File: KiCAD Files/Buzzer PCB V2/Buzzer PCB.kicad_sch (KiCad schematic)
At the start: 18 parts, among them J1 2600mAh LiPo JST-PH bottom, J10 Adafruit ESP32 Feather V2, J11 OLED FeatherWing, J2 Legacy SW_BAT/GND out, J3 SD card module 18x18 swapped, J4 Legacy D13 test pad, J5 GPS M100 Mini 15x15, J6 BMP390/BMP5xx top pads, J7 SHT41 top pads, Q1 S8050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

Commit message: V2 with sparkfun
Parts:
- removed J10: Adafruit ESP32 Feather V2, Vario_Buzzer_V2:Feather_28_Header_Separate, symbol Vario_Buzzer_V2:Feather_28_Header
- removed J11: OLED FeatherWing, Vario_Buzzer_V2:OLED_FeatherWing_28_Header, symbol Vario_Buzzer_V2:Feather_28_Header
- added J10: SparkFun Thing Plus ESP32 WROOM-C USB-C, Vario_Buzzer_V2:SparkFun_Thing_Plus_ESP32_WROOM_C_Header, symbol Vario_Buzzer_V2:SparkFun_Thing_Plus_ESP32_WROOM_C
- added J11: SparkFun Qwiic OLED 1.3in, Vario_Buzzer_V2:SparkFun_Qwiic_OLED_1p3_Module, symbol Vario_Buzzer_V2:SparkFun_Qwiic_OLED_1p3
- added SW2: BACK, Vario_Buzzer_V2:Ant_Display_SW_PUSH_6mm_H5mm, symbol Vario_Buzzer_V2:Ant_Display_Button
- added SW3: NEXT, Vario_Buzzer_V2:Ant_Display_SW_PUSH_6mm_H5mm, symbol Vario_Buzzer_V2:Ant_Display_Button
- added SW4: DOWN, Vario_Buzzer_V2:Ant_Display_SW_PUSH_6mm_H5mm, symbol Vario_Buzzer_V2:Ant_Display_Button
- added SW5: UP, Vario_Buzzer_V2:Ant_Display_SW_PUSH_6mm_H5mm, symbol Vario_Buzzer_V2:Ant_Display_Button
- J3: value SD card module 18x18 swapped -> Optional SD module 18x18 swapped
- J5: value GPS M100 Mini 15x15 -> HGLRC M100 Mini GPS
- SW1: value SS12D00G5 -> SS12D00G5 power switch
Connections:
- net GPS_RX_FEATHER_TX is gone; now on net GND: J5.1 (RX)
- net GPS_TX_FEATHER_RX is gone; now on net 3V3: J5.2 (TX)
- net 3V3: now also J11.3 (SDA); no longer J5.3 (TX)
- net GND: now also SW1.1 (ON), J11.4 (SCL), SW2.1 (BTN), SW3.1 (BTN), SW4.1 (BTN), SW5.1 (BTN); no longer J5.4 (RX)
- net SCL: now also J11.1 (GND)
- net SDA: now also J11.2 (VDD/3V3)
- net D13 renamed D13_BUZZER_GPIO13
- net D13_BUZZER_GPIO13: now also J10.15 (RX ESP16)
- net SD_CS_D10_IO27 renamed SD_CS_GPIO2
- net SD_CS_GPIO2: now also J10.23 (A1/ESP25)
- new net BTN_BACK_GPIO3: J10.19 (A5/ESP35), SW2.2 (GND)
- new net BTN_DOWN_GPIO5: J10.21 (A3/ESP39), SW4.2 (GND)
- new net BTN_NEXT_GPIO4: J10.20 (A4/ESP36), SW3.2 (GND)
- new net BTN_UP_GPIO21: J10.22 (A2/ESP34), SW5.2 (GND)
- new net GPS_RX_THING_TX: J10.14 (TX ESP17), J5.4 (GND)
- new net GPS_TX_THING_RX: J10.9 (D13/ESP13 STAT), J5.3 (VCC)
- no-connect marks 36 -> 2
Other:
- note added: "Ant Display tactile switch pad geometry and button net names are copied; UP net is routed to Thing FREEBIE/ESP4 to keep SDA free for I2C."
- note added: "Buzzer circuit and copied original Buzzer PCB passives/JST/slide-switch footprints are preserved; PCB remains placement-only with no traces."
- note added: "HGLRC M100 footprint uses manual pad order RX TX VCC GND; VCC is tied to 3V3 per HGLRC 3.3V-5V product spec."
- note added: "SparkFun Thing Plus and SparkFun Qwiic OLED replace the Feather/FeatherWing. OLED uses direct 3V3/GND/SDA/SCL pads; no PCB Qwiic port is placed."
- note added: "SparkFun Thing Plus pinout and module outline are from SparkFun Eagle hardware. Onboard microSD exists; J3 is optional external SPI SD using GPIO2 as CS."
- note removed: "BMP/SHT footprints use Adafruit EagleCAD breakout geometry; top-facing modules solder from PCB backside."
- note removed: "J3 SD pin order is reversed: 1 GND, 2 MISO, 3 CLK, 4 MOSI, 5 CS, 6 3V3."
- note removed: "Reused buzzer/JST/switch/passive footprints and pad nets are copied from the original Buzzer PCB board file."
- note removed: "U1 TP4057: USB-C edge is opposite BAT+/BAT- pads. BAT_IN charges before SW1; SW_BAT feeds Feather VBAT and buzzer."
- note removed: "V2 separates Feather and OLED FeatherWing onto J10/J11. No separate I2C cable connector is placed on this PCB."
- title: Feather Vario Buzzer / Sensor Interposer PCB V2 -> SparkFun Thing Plus Vario Buzzer / Sensor Interposer PCB V2

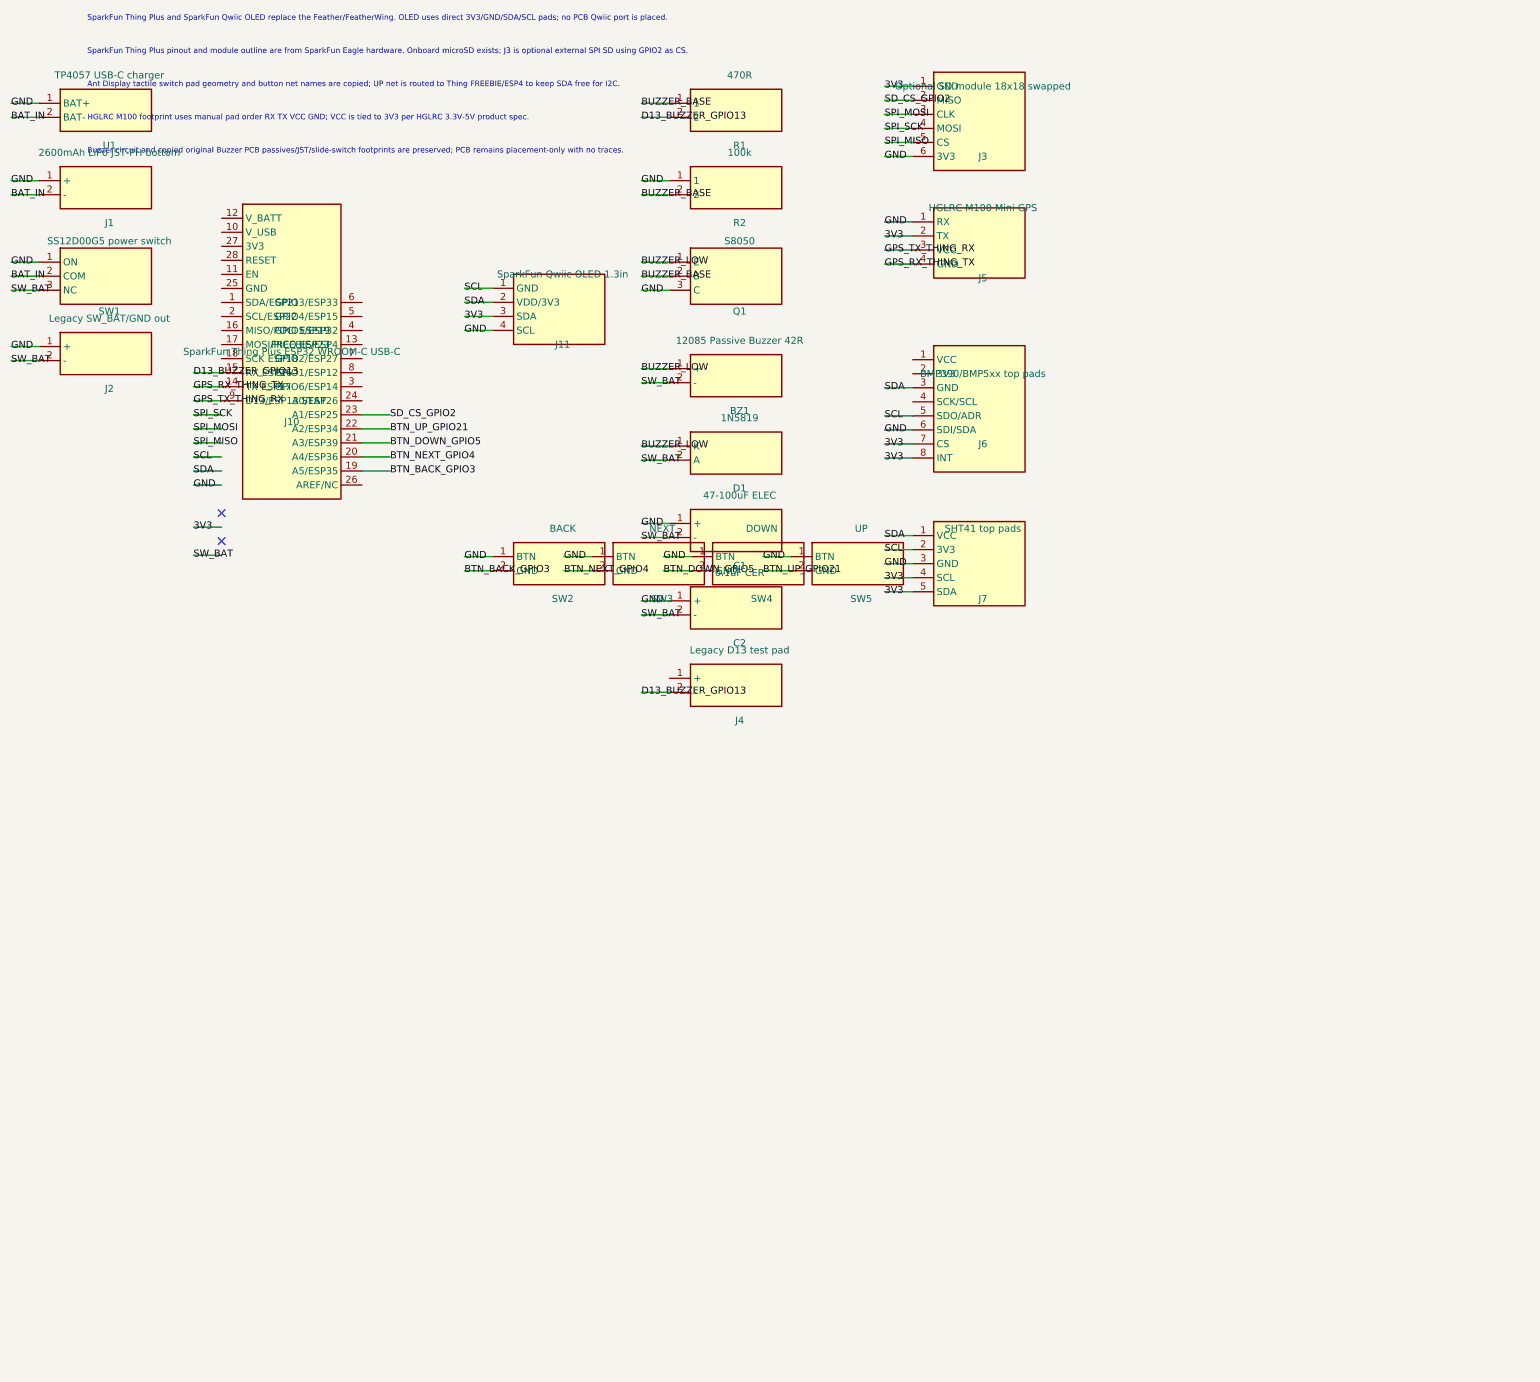
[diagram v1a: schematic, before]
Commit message: Restore KiCad component references and footprints
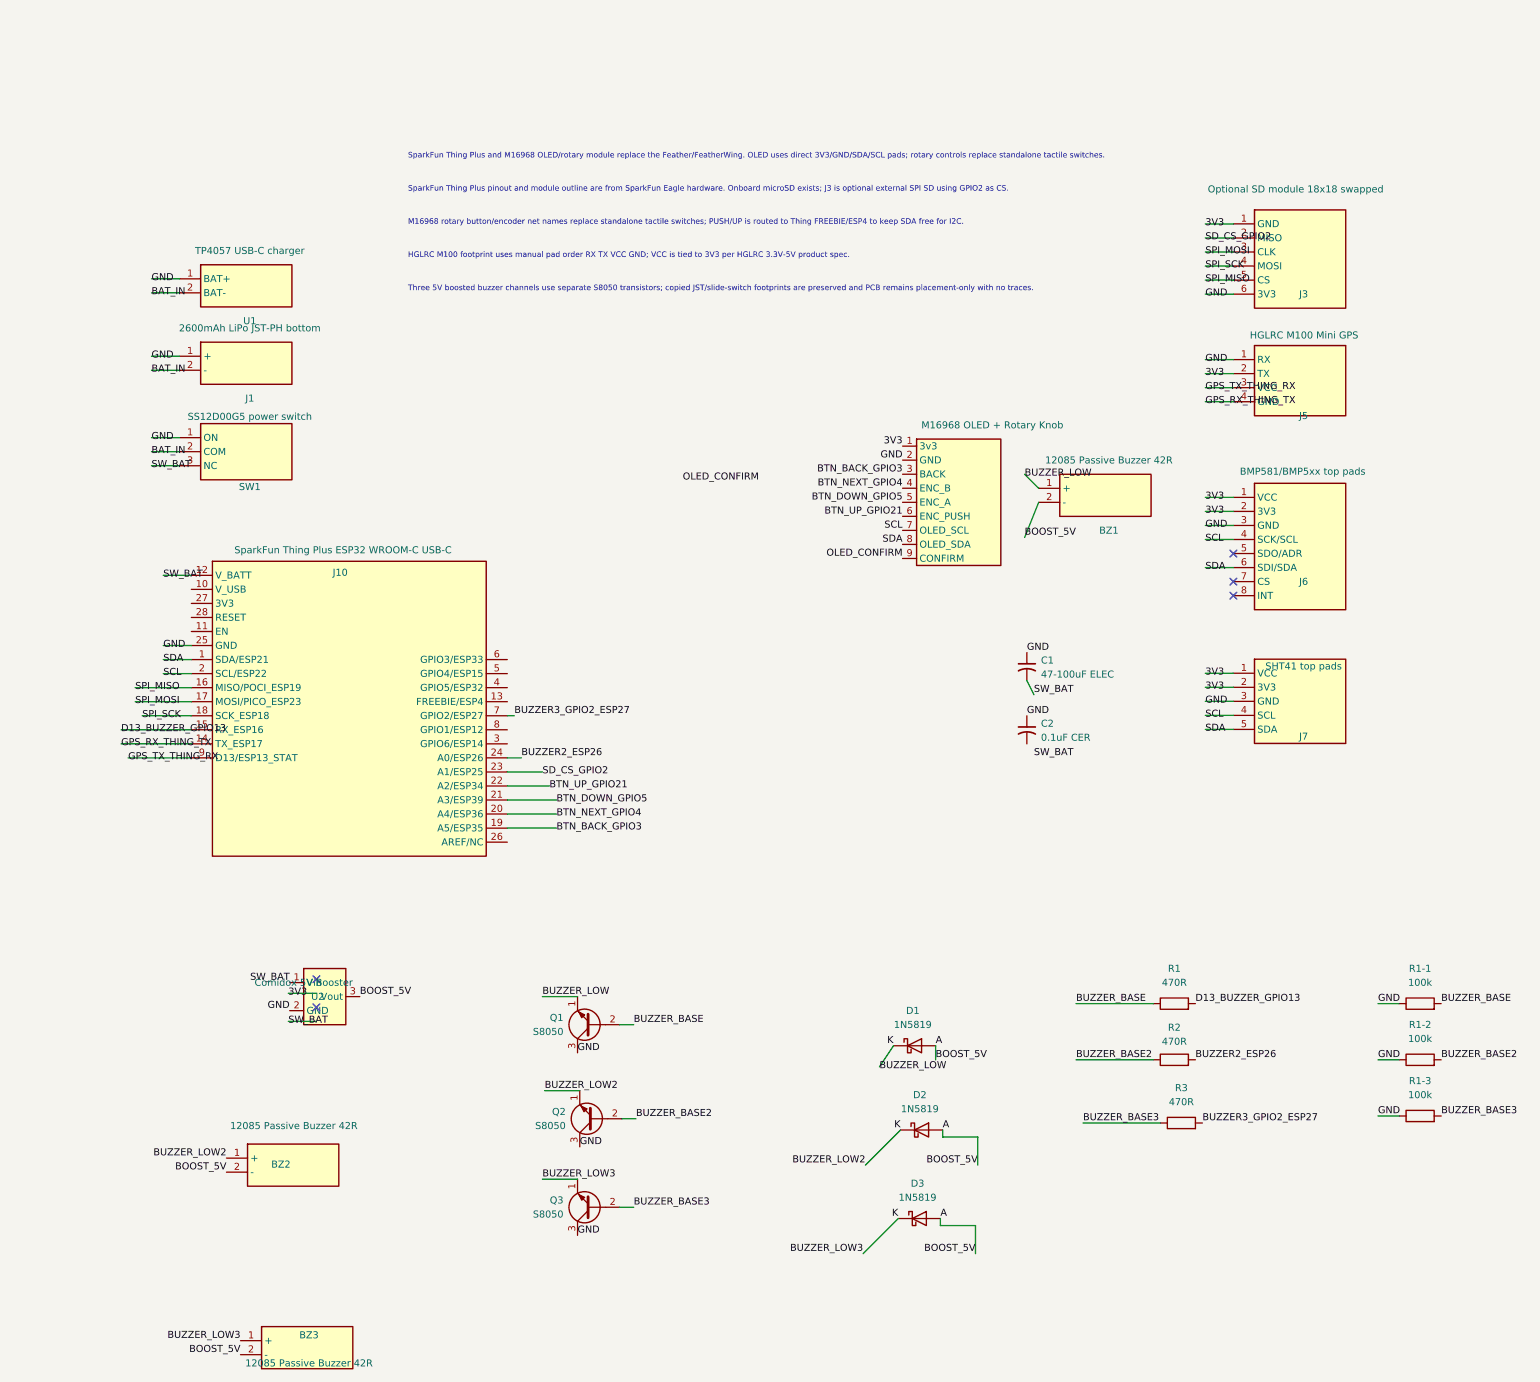
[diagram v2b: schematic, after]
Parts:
- removed C1: 47-100uF ELEC, Capacitor_THT:CP_Radial_D5.0mm_P2.00mm, symbol Vario_Buzzer_V2:Capacitor_2
- removed C2: 0.1uF CER, Capacitor_THT:C_Disc_D3.0mm_W1.6mm_P2.50mm, symbol Vario_Buzzer_V2:Capacitor_2
- removed D1: 1N5819, Diode_THT:D_DO-41_SOD81_P10.16mm_Horizontal, symbol Vario_Buzzer_V2:Diode_2
- removed J11: SparkFun Qwiic OLED 1.3in, Vario_Buzzer_V2:SparkFun_Qwiic_OLED_1p3_Module, symbol Vario_Buzzer_V2:SparkFun_Qwiic_OLED_1p3
- removed J2: Legacy SW_BAT/GND out, Connector_JST:JST_PH_S2B-PH-K_1x02_P2.00mm_Horizontal, symbol Vario_Buzzer_V2:Conn_2
- removed J4: Legacy D13 test pad, Connector_PinHeader_2.54mm:PinHeader_1x01_P2.54mm_Vertical, symbol Vario_Buzzer_V2:Conn_2
- removed Q1: S8050, Package_TO_SOT_THT:TO-92_Inline_Wide_Formed, symbol Vario_Buzzer_V2:NPN_EBC_3
- removed R1: 470R, Resistor_THT:R_Axial_DIN0207_L6.3mm_D2.5mm_P7.62mm_Horizontal, symbol Vario_Buzzer_V2:Resistor_2
- removed R2: 100k, Resistor_THT:R_Axial_DIN0207_L6.3mm_D2.5mm_P7.62mm_Horizontal, symbol Vario_Buzzer_V2:Resistor_2
- removed SW2: BACK, Vario_Buzzer_V2:Ant_Display_SW_PUSH_6mm_H5mm, symbol Vario_Buzzer_V2:Ant_Display_Button
- removed SW3: NEXT, Vario_Buzzer_V2:Ant_Display_SW_PUSH_6mm_H5mm, symbol Vario_Buzzer_V2:Ant_Display_Button
- removed SW4: DOWN, Vario_Buzzer_V2:Ant_Display_SW_PUSH_6mm_H5mm, symbol Vario_Buzzer_V2:Ant_Display_Button
- removed SW5: UP, Vario_Buzzer_V2:Ant_Display_SW_PUSH_6mm_H5mm, symbol Vario_Buzzer_V2:Ant_Display_Button
- added BZ2, BZ3: 12085 Passive Buzzer 42R, Buzzer_Beeper:Buzzer_12x8.5mm_P7.62mm_Custom, symbol Vario_Buzzer_V2:Buzzer_2
- added C1: 47-100uF ELEC, Capacitor_THT:CP_Radial_D5.0mm_P2.00mm, symbol Device:C_Small_US
- added C2: 0.1uF CER, Vario_Buzzer_V2:Ceramic_Cap_0.1uF_P5.00mm_V1, symbol Device:C_Small_US
- added D1, D2, D3: 1N5819, Diode_THT:D_DO-41_SOD81_P10.16mm_Horizontal, symbol Diode:1N5819
- added J11: M16968 OLED + Rotary Knob, Vario_Buzzer_V2:OLED_M16968_59x35_9Pin, symbol Vario_Buzzer_V2:M16968_OLED_RotaryKnob_9
- added Q1, Q2, Q3: S8050, Package_TO_SOT_THT:TO-92_Inline, symbol Transistor_BJT:S8050
- added R1, R2, R3: 470R, Resistor_THT:R_Axial_DIN0207_L6.3mm_D2.5mm_P10.16mm_Horizontal, symbol Device:R
- added R1-1, R1-2, R1-3: 100k, Resistor_THT:R_Axial_DIN0207_L6.3mm_D2.5mm_P10.16mm_Horizontal, symbol Device:R
- added U2: Comidox 5V Booster, Vario_Buzzer_V2:Comidox_5V_Booster_10.75x10.75_3Pin, symbol Vario_Buzzer_V2:Comidox_5V_Booster_3
- J6: value BMP390/BMP5xx top pads -> BMP581/BMP5xx top pads
- U1: footprint Vario_Buzzer_V2:TP4057_Module_18.2x12.3 -> Vario_Buzzer_V2:TP4057_Module_12.2x18.5
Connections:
- net 3V3: now also J6.1 (VCC), J6.2 (3V3), J7.1 (VCC), J7.2 (3V3), J11.1 (3v3); no longer J6.7 (CS), J6.8 (INT), J7.4 (SCL), J7.5 (SDA)
- net BTN_BACK_GPIO3: now also J11.3 (BACK)
- net BTN_DOWN_GPIO5: now also J11.5 (ENC_A)
- net BTN_NEXT_GPIO4: now also J11.4 (ENC_B)
- net BTN_UP_GPIO21: now also J11.6 (ENC_PUSH)
- net BUZZER_BASE: now also Q1.2 (B), R1-1.2, R1.1
- net BUZZER_LOW: now also BZ2.1 (+), BZ3.1 (+), D1.1 (K), D2.1 (K), D3.1 (K), Q1.1 (E), Q2.1 (E), Q3.1 (E)
- net D13_BUZZER_GPIO13: now also R1.2
- net GND: now also J10.25 (GND), J6.3 (GND), C1.1, C2.1, J11.2 (GND), Q1.3 (C), Q2.3 (C), Q3.3 (C), R1-1.1, R1-2.1, R1-3.1, U2.2 (GND); no longer J6.6 (SDI/SDA)
- net SCL: now also J10.2 (SCL/ESP22), J6.4 (SCK/SCL), J7.4 (SCL), J11.7 (OLED_SCL); no longer J6.5 (SDO/ADR), J7.2 (3V3)
- net SDA: now also J10.1 (SDA/ESP21), J6.6 (SDI/SDA), J7.5 (SDA), J11.8 (OLED_SDA); no longer J6.3 (GND), J7.1 (VCC)
- net SPI_MISO: now also J10.16 (MISO/POCI_ESP19)
- net SPI_MOSI: now also J10.17 (MOSI/PICO_ESP23)
- net SPI_SCK: now also J10.18 (SCK_ESP18)
- net SW_BAT: now also J10.12 (V_BATT), C1.2, U2.1 (Vin); no longer BZ1.2 (-)
- net BUZZER2_ESP26: now reaches J10.24 (A0/ESP26)
- net BUZZER2_ESP26: now also R2.2
- net BUZZER3_GPIO2_ESP27: now reaches J10.7 (GPIO2/ESP27)
- net BUZZER3_GPIO2_ESP27: now also R3.2
- new net A: BZ1.2 (-), BZ2.2 (-), BZ3.2 (-), D1.2 (A), D2.2 (A), D3.2 (A), U2.3 (Vout)
- new net BUZZER_BASE2: Q2.2 (B), R1-2.2, R2.1
- new net BUZZER_BASE3: Q3.2 (B), R1-3.2, R3.1
- new net OLED_CONFIRM: J11.9 (CONFIRM)
- no-connect marks 2 -> 5
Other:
- note added: "M16968 rotary button/encoder net names replace standalone tactile switches; PUSH/UP is routed to Thing FREEBIE/ESP4 to keep SDA free for I2C."
- note added: "SparkFun Thing Plus and M16968 OLED/rotary module replace the Feather/FeatherWing. OLED uses direct 3V3/GND/SDA/SCL pads; rotary controls replace standalone tactile switches."
- note added: "Three 5V boosted buzzer channels use separate S8050 transistors; copied JST/slide-switch footprints are preserved and PCB remains placement-only with no traces."
- note removed: "Ant Display tactile switch pad geometry and button net names are copied; UP net is routed to Thing FREEBIE/ESP4 to keep SDA free for I2C."
- note removed: "Buzzer circuit and copied original Buzzer PCB passives/JST/slide-switch footprints are preserved; PCB remains placement-only with no traces."
- note removed: "SparkFun Thing Plus and SparkFun Qwiic OLED replace the Feather/FeatherWing. OLED uses direct 3V3/GND/SDA/SCL pads; no PCB Qwiic port is placed."
- moved on the sheet: BZ1, J1, J10, J3, J5, J6, J7, SW1, U1

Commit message: asd
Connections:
- net 3V3: no longer J6.2 (3V3), J7.2 (3V3)
- net OLED_CONFIRM: now also J10.13 (FREEBIE/ESP4)
- no-connect marks 5 -> 6
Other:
- moved on the sheet: BZ1, BZ2
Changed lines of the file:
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@@
 	)
 	(no_connect
+		(at 62.23 223.52)
+	)
+	(no_connect
 		(at 59.45 191.17)
 	)
@@
 	(wire
 		(pts
-			(xy 187.55 111.26) (xy 190.09 104.91)
+			(xy 44.45 233.68) (xy 46.99 227.33)
 		)
 		(stroke
@@
 	(wire
 		(pts
-			(xy 187.55 99.83) (xy 190.09 102.37)
+			(xy 44.45 222.25) (xy 46.99 224.79)
 		)
 		(stroke
@@
 	(wire
 		(pts
+			(xy 43.18 242.57) (xy 43.18 241.3)
+		)
+		(stroke
+			(width 0)
+			(type default)
+		)
+	)
+	(wire
+		(pts
 			(xy 31.75 135.89) (xy 36.83 135.89)
 		)
@@
 	(wire
 		(pts
-			(xy 178.66 235.72) (xy 172.31 235.72)
+			(xy 48.26 242.57) (xy 43.18 242.57)
 		)
 		(stroke
@@
 	(wire
 		(pts
-			(xy 178.66 240.8) (xy 178.66 235.72)
+			(xy 178.66 235.72) (xy 172.31 235.72)
 		)
 		(stroke
@@
 	(wire
 		(pts
-			(xy 116.84 199.39) (xy 114.3 199.39)
+			(xy 178.66 240.8) (xy 178.66 235.72)
 		)
 		(stroke
@@
 	(wire
 		(pts
-			(xy 172.72 219.71) (xy 172.72 218.44)
+			(xy 116.84 199.39) (xy 114.3 199.39)
 		)
 		(stroke
@@
 	(wire
 		(pts
-			(xy 29.62 95.75) (xy 34.7 95.75)
+			(xy 172.72 219.71) (xy 172.72 218.44)
 		)
 		(stroke
@@
 	(wire
 		(pts
-			(xy 196.85 195.58) (xy 210.82 195.58)
+			(xy 43.18 246.38) (xy 48.26 245.11)
 		)
 		(stroke
@@
 	(wire
 		(pts
-			(xy 158.34 240.8) (xy 164.69 234.45)
+			(xy 29.62 95.75) (xy 34.7 95.75)
 		)
 		(stroke
@@
 	(wire
 		(pts
-			(xy 220.23 59.63) (xy 225.31 59.63)
+			(xy 196.85 195.58) (xy 210.82 195.58)
 		)
 		(stroke
@@
 	(wire
 		(pts
-			(xy 29.62 64.48) (xy 34.7 64.48)
+			(xy 158.34 240.8) (xy 164.69 234.45)
 		)
 		(stroke
@@
 	(wire
 		(pts
-			(xy 220.23 138.36) (xy 225.31 138.36)
+			(xy 220.23 59.63) (xy 225.31 59.63)
 		)
 		(stroke
@@
 	(wire
 		(pts
-			(xy 220.23 104.01) (xy 225.31 104.01)
+			(xy 29.62 64.48) (xy 34.7 64.48)
 		)
 		(stroke
@@
 	(wire
 		(pts
-			(xy 220.23 106.55) (xy 225.31 106.55)
+			(xy 220.23 104.01) (xy 225.31 104.01)
 		)
 		(stroke
@@
 		)
 	)
-	(label "3V3"
-		(at 220.23 138.36 0)
-		(effects
-			(font
-				(size 1.27 1.27)
-			)
-		)
-	)
 	(label "BUZZER_BASE"
 		(at 262.89 195.58 0)
@@
 		)
 	)
-	(label "3V3"
-		(at 220.23 106.55 0)
-		(effects
-			(font
-				(size 1.27 1.27)
-			)
-		)
-	)
 	(label "BOOST_5V"
 		(at 171.45 205.74 0)
@@
 	)
 	(label "BUZZER_LOW"
-		(at 187.55 99.83 0)
+		(at 44.45 222.25 0)
 		(effects
 			(font
@@
 	)
 	(label "BOOST_5V"
-		(at 187.55 111.26 0)
+		(at 44.45 233.68 0)
 		(effects
 			(font
@@
 	)
 	(label "BUZZER_LOW2"
-		(at 43.18 223.52 180)
+		(at 43.18 241.3 180)
 		(effects
 			(font
@@
 	)
 	(label "BOOST_5V"
-		(at 43.18 226.06 180)
+		(at 43.18 246.38 180)
 		(effects
 			(font
@@
 		)
 	)
+	(label "OLED_CONFIRM"
+		(at 93.98 140.97 0)
+		(effects
+			(font
+				(size 1.27 1.27)
+			)
+			(justify left bottom)
+		)
+	)
 	(label "BUZZER_BASE"
 		(at 196.85 195.58 0)
@@
 	(symbol
 		(lib_id "Vario_Buzzer_V2:Buzzer_2")
-		(at 202.79 103.64 0)
+		(at 59.69 226.06 0)
 		(unit 1)
 		(body_style 1)
@@
 		(dnp no)
 		(property "Reference" "BZ1"
-			(at 202.79 109.99 0)
+			(at 59.69 232.41 0)
 			(show_name no)
 			(do_not_autoplace no)
@@
 		)
 		(property "Value" "12085 Passive Buzzer 42R"
-			(at 202.79 97.29 0)
+			(at 59.436 218.948 0)
 			(show_name no)
 			(do_not_autoplace no)
@@
 		)
 		(property "Footprint" "Buzzer_Beeper:Buzzer_12x8.5mm_P7.62mm_Custom"
-			(at 202.79 103.64 0)
+			(at 59.69 226.06 0)
 			(hide yes)
 			(show_name no)
@@
 		)
 		(property "Datasheet" ""
-			(at 66.79 21.64 0)
+			(at -76.31 144.06 0)
 			(hide yes)
 			(show_name no)
@@
 		)
 		(property "Description" ""
-			(at 202.79 103.64 0)
+			(at 59.69 226.06 0)
 			(show_name no)
 			(do_not_autoplace no)
@@
 		)
 		(property "Value" "12085 Passive Buzzer 42R"
-			(at 58.11 260.61 0)
+			(at 57.15 251.968 0)
 			(show_name no)
 			(do_not_autoplace no)
@@
 	(symbol
 		(lib_id "Vario_Buzzer_V2:Buzzer_2")
-		(at 55.88 224.79 0)
+		(at 60.96 243.84 0)
 		(unit 1)
 		(body_style 1)
@@
 		(dnp no)
 		(property "Reference" "BZ2"
-			(at 53.03 224.65 0)
+			(at 58.11 243.7 0)
 			(show_name no)
 			(do_not_autoplace no)
@@
 		)
 		(property "Value" "12085 Passive Buzzer 42R"
-			(at 55.372 217.678 0)
+			(at 59.436 237.744 0)
 			(show_name no)
 			(do_not_autoplace no)
@@
 		)
 		(property "Footprint" "Buzzer_Beeper:Buzzer_12x8.5mm_P7.62mm_Custom"
-			(at 55.88 224.79 0)
+			(at 60.96 243.84 0)
 			(hide yes)
 			(show_name no)
@@
 		)
 		(property "Datasheet" "~"
-			(at 55.88 224.79 0)
+			(at 60.96 243.84 0)
 			(hide yes)
 			(show_name no)
@@
 		)
 		(property "Description" ""
-			(at 55.88 224.79 0)
+			(at 60.96 243.84 0)
 			(show_name no)
 			(do_not_autoplace no)
